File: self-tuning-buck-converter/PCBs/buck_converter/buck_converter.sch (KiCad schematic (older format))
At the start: 35 parts, among them Q1 NMOS, U1 LT1999-50, U2 LM7322, U3 IR2125, U4 ESP32-DEVKITC-32D

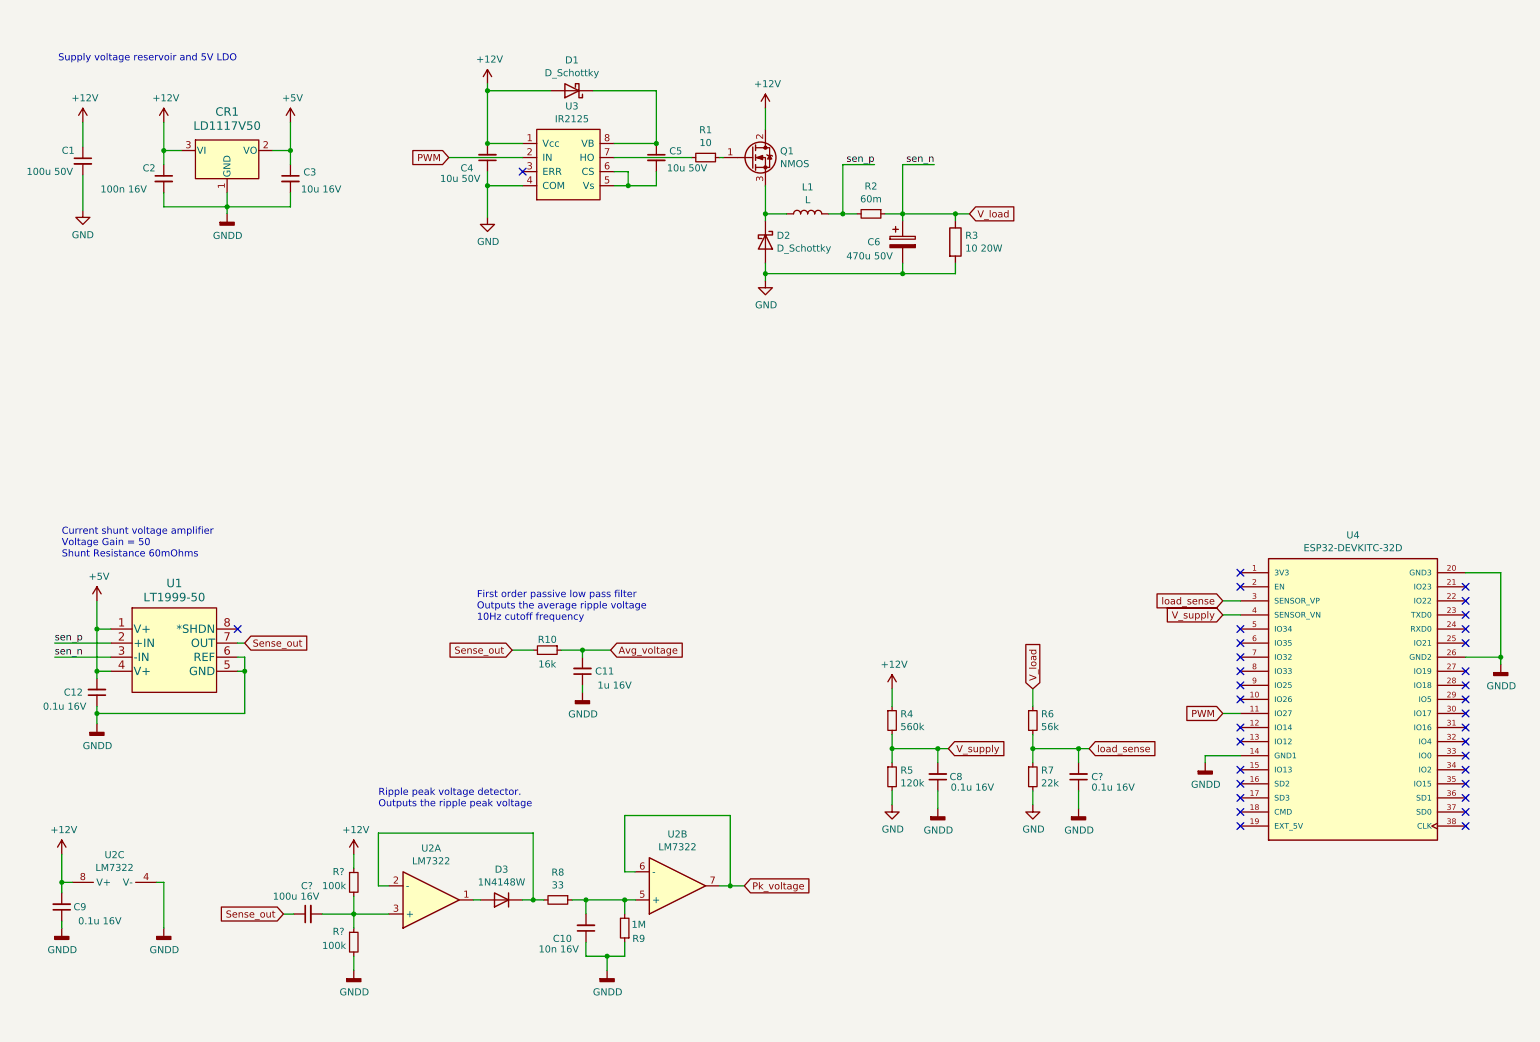
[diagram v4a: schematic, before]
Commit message: Finalised PCM and selected component footprints
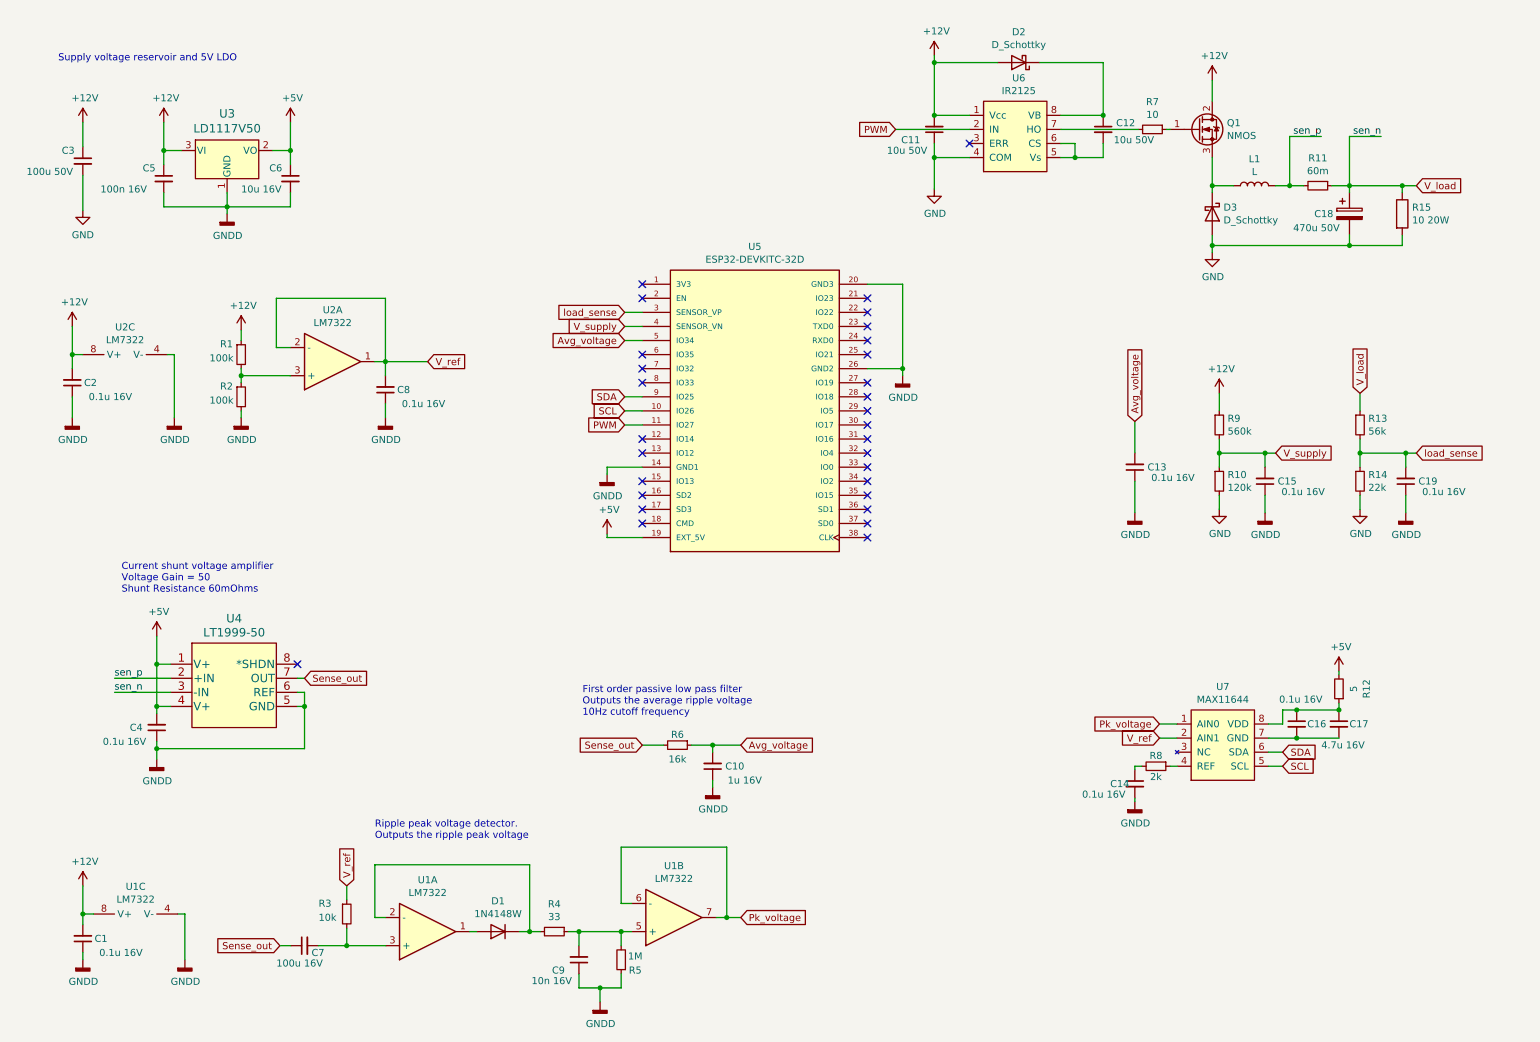
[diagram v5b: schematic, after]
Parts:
- removed CR1: LD1117V50, TO-220_STM, symbol LD1117V50:LD1117V50
- added C13, C14, C16, C2, C8: 0.1u 16V, Capacitor_SMD:C_0603_1608Metric_Pad1.08x0.95mm_HandSolder, symbol Device:C_Small
- added C17: 4.7u 16V, Capacitor_SMD:C_0603_1608Metric_Pad1.08x0.95mm_HandSolder, symbol Device:C_Small
- added R12: 5, Resistor_SMD:R_0603_1608Metric_Pad0.98x0.95mm_HandSolder, symbol Device:R_Small
- added R3: 10k, Resistor_SMD:R_0603_1608Metric_Pad0.98x0.95mm_HandSolder, symbol Device:R_Small
- added R8: 2k, Resistor_SMD:R_0603_1608Metric_Pad0.98x0.95mm_HandSolder, symbol Device:R_Small
- added U2: LM7322, Package_SO:SOIC-8_3.9x4.9mm_P1.27mm, symbol Device:Opamp_Dual_Generic
- added U3: LD1117V50, Package_TO_SOT_THT:TO-220-3_Vertical, symbol LD1117V50:LD1117V50
- added U7: MAX11644, Package_SO:MSOP-8_3x3mm_P0.65mm, symbol MAX11644:MAX11644
- C1: renamed from C9; footprint (none) -> Capacitor_SMD:C_0603_1608Metric_Pad1.08x0.95mm_HandSolder
- C10: renamed from C11; footprint (none) -> Capacitor_SMD:C_0603_1608Metric_Pad1.08x0.95mm_HandSolder
- C11: renamed from C4; footprint (none) -> Capacitor_THT:CP_Radial_D5.0mm_P2.00mm; Part Number (none) -> 860010672009
- C12: renamed from C5; footprint (none) -> Capacitor_THT:CP_Radial_D5.0mm_P2.00mm; Part Number (none) -> 860010672009
- C15: renamed from C8; footprint (none) -> Capacitor_SMD:C_0603_1608Metric_Pad1.08x0.95mm_HandSolder
- C19: renamed from C?; footprint (none) -> Capacitor_SMD:C_0603_1608Metric_Pad1.08x0.95mm_HandSolder
- C3: renamed from C1; footprint (none) -> Capacitor_THT:CP_Radial_D10.0mm_P5.00mm; Part Number (none) -> 860010675020
- C4: renamed from C12; footprint (none) -> Capacitor_SMD:C_0603_1608Metric_Pad1.08x0.95mm_HandSolder
- C5: renamed from C2; footprint (none) -> Capacitor_SMD:C_0603_1608Metric_Pad1.08x0.95mm_HandSolder
- C6: renamed from C3; footprint (none) -> Capacitor_SMD:C_0805_2012Metric_Pad1.18x1.45mm_HandSolder
- C7: renamed from C?; footprint (none) -> Capacitor_THT:CP_Radial_D8.0mm_P3.50mm; Part Number (none) -> 860020374012
- C9: renamed from C10; footprint (none) -> Capacitor_SMD:C_0603_1608Metric_Pad1.08x0.95mm_HandSolder
- D1: renamed from D3; footprint Diode_SMD:D_SOD-123 -> Diode_THT:D_DO-35_SOD27_P7.62mm_Horizontal
- D2: renamed from D1; footprint (none) -> Diode_THT:D_A-405_P12.70mm_Horizontal
- D3: renamed from D2; footprint (none) -> Diode_THT:D_A-405_P12.70mm_Horizontal
- Q1: footprint (none) -> Package_TO_SOT_THT:TO-220-3_Vertical
- R1, R2: renamed from R?; footprint (none) -> Resistor_SMD:R_0603_1608Metric_Pad0.98x0.95mm_HandSolder
- R10: renamed from R5; footprint (none) -> Resistor_SMD:R_0603_1608Metric_Pad0.98x0.95mm_HandSolder
- R13: renamed from R6; footprint (none) -> Resistor_SMD:R_0603_1608Metric_Pad0.98x0.95mm_HandSolder
- R14: renamed from R7; footprint (none) -> Resistor_SMD:R_0603_1608Metric_Pad0.98x0.95mm_HandSolder
- R4: renamed from R8; footprint (none) -> Resistor_SMD:R_0603_1608Metric_Pad0.98x0.95mm_HandSolder
- R5: renamed from R9; footprint (none) -> Resistor_SMD:R_0603_1608Metric_Pad0.98x0.95mm_HandSolder
- R7: renamed from R1; footprint (none) -> Resistor_SMD:R_0603_1608Metric_Pad0.98x0.95mm_HandSolder
- R9: renamed from R4; footprint (none) -> Resistor_SMD:R_0603_1608Metric_Pad0.98x0.95mm_HandSolder
- U1: renamed from U2; footprint (none) -> Package_SO:SOIC-8_3.9x4.9mm_P1.27mm
- U4: renamed from U1; footprint MSOP_8_ADI -> Package_SO:SOIC-8_3.9x4.9mm_P1.27mm
- U6: renamed from U3; footprint (none) -> Package_DIP:DIP-8_W7.62mm
- renumbered C6 to C18, R2 to R11, R3 to R15, R10 to R6, U4 to U5
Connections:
- net +12V: now also C2.2, U2.8 (V+), U3.3 (VI)
- net +5V: now also U5.19 (EXT_5V), R12.2, U3.2 (VO)
- net Avg_voltage: now also U5.5 (IO34), C13.2
- net GNDD: now also C13.1, C14.2, C2.1, C8.1, U2.4 (V-), U3.1 (GND)
- net Pk_voltage: now also U7.1 (AIN0)
- net SCL: now reaches U5.10 (IO26)
- net SCL: now also U7.5 (SCL)
- net SDA: now reaches U5.9 (IO25)
- net SDA: now also U7.6 (SDA)
- net at R1.2, R2.1: now also U2.3 (+); no longer C7.2, U1.3 (+)
- new net: C7.2, R3.2, U1.3 (+)
- new net: R8.1, U7.4 (REF)
- new net: C16.2, C17.2, U7.7 (GND)
- new net: C16.1, C17.1, R12.1, U7.8 (VDD)
- new net: C14.1, R8.2
- new net V_ref: C8.2, R3.1, U2.1, U2.2 (-), U7.2 (AIN1)
- no-connect marks 34 -> 30
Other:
- moved on the sheet: C1, C10, C11, C12, C15, C18, C19, C4, C7, C9, D1, D2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

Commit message: Updated schematic with edits found from building it in the lab
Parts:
- removed R4: 33, Resistor_SMD:R_0603_1608Metric_Pad0.98x0.95mm_HandSolder, symbol Device:R_Small
- removed unit 2 of U1
- removed U2: LM7322, Package_SO:SOIC-8_3.9x4.9mm_P1.27mm, symbol Device:Opamp_Dual_Generic
- added RV1: 100, Potentiometer_THT:Potentiometer_Bourns_3266Y_Vertical, symbol Device:R_POT
- added U1: AMP from lab, Package_DIP:DIP-14_W7.62mm, symbol Device:Opamp_Quad_Generic
- C11, C12: symbol Device:C_Small -> Device:CP_Small
- C9: value 10n 16V -> 100n 16V
- D2, D3: footprint Diode_THT:D_A-405_P12.70mm_Horizontal -> Diode_THT:D_A-405_P7.62mm_Horizontal
- renumbered C2 to C1, C18 to C16, C16 to C17, C19 to C18, C17 to C19, C4 to C2, C1 to C4, R11 to R10, R13 to R11, R14 to R12, R15 to R13, R12 to R14, R5 to R4, R6 to R5, R7 to R6, R9 to R7, R10 to R8, R8 to R9, U1 to U2, U4 to U3, U3 to U4, U5 to U6, U6 to U7, U7 to U8
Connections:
- net +12V: now also C11.1, U1.11 (V-); no longer C11.2
- net GND: now also C11.2; no longer C11.1
- net GNDD: now also U1.4 (V+)
- net Pk_voltage: now also U1.5 (+), U1.7
- net V_ref: now also U1.1, U1.3 (+)
- net at D3.1 (K), L1.1, Q1.3 (S): now also C12.2, U7.5 (Vs), U7.6 (CS)
- net at R1.2, R2.1: now also U1.2 (-)
- net at D1.1 (K), U2.2 (-): now also RV1.1
- net at C9.2, R4.2: now also RV1.2, U1.6 (-)
- no-connect marks 30 -> 31
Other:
- note added: "Supply voltage (VCC) reservoir, 5V LDO, and VCC/2 refrence voltage"
- note removed: "Supply voltage reservoir and 5V LDO"
- moved on the sheet: C1, C10, C13, C14, C15, C16, C17, C18, C19, C2, C3, C5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

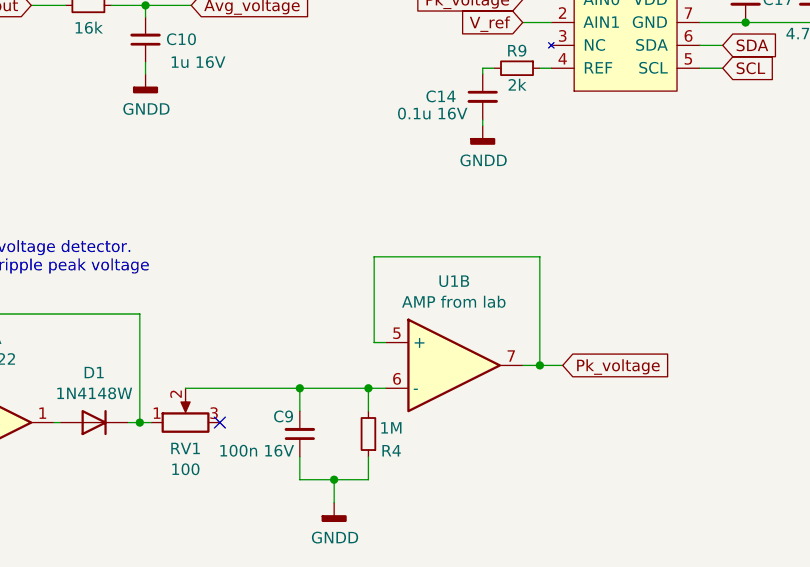
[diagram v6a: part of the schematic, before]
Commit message: PEak detection evaluation
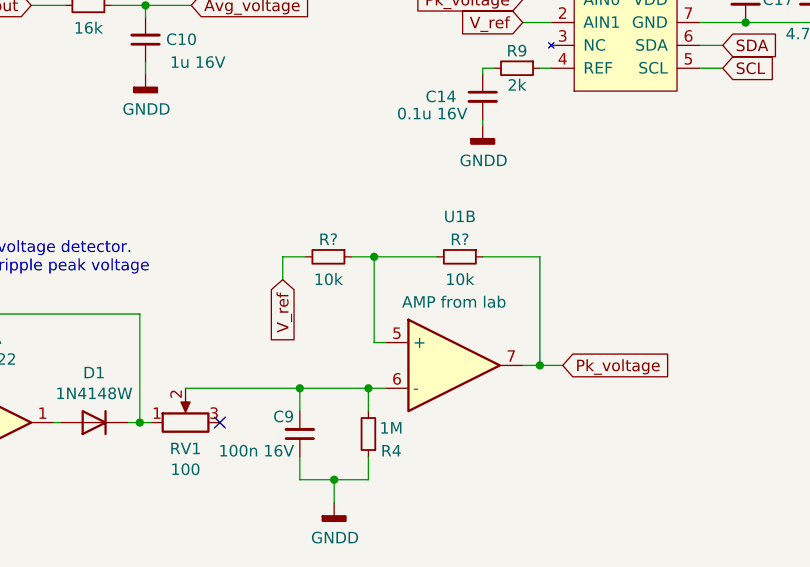
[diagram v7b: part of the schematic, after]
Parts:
- added R? (x2): 10k, Resistor_SMD:R_0603_1608Metric_Pad0.98x0.95mm_HandSolder, symbol Device:R_Small
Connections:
- net Pk_voltage: now also R?.1; no longer U1.5 (+)
- net V_ref: now also R?.2
- new net: R?.1, R?.2, U1.5 (+)
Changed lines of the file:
@@
 U 2 1 6162B04C
 P 5475 6800
-F 0 "U1" H 5475 7167 50  0000 C CNN
+F 0 "U1" H 5500 7450 50  0000 C CNN
 F 1 "AMP from lab" H 5475 7076 50  0000 C CNN
 F 2 "Package_DIP:DIP-14_W7.62mm" H 5475 6800 50  0001 C CNN
@@
 Wire Wire Line
 	5850 6800 5850 6325
-Wire Wire Line
-	5850 6325 5125 6325
 Wire Wire Line
 	5775 6800 5850 6800
@@
 Connection ~ 5300 3350
 Connection ~ 6175 3350
+$Comp
+L Device:R_Small R?
+U 1 1 6151C957
+P 4925 6325
+F 0 "R?" V 4850 6325 50  0000 C CNN
+F 1 "10k" V 5025 6325 50  0000 C CNN
+F 2 "Resistor_SMD:R_0603_1608Metric_Pad0.98x0.95mm_HandSolder" H 4925 6325 50  0001 C CNN
+F 3 "~" H 4925 6325 50  0001 C CNN
+F 4 "RR0816P-163-D" V 4925 6325 50  0001 C CNN "Part Number"
+	1    4925 6325
+	0    1    1    0
+$EndComp
+$Comp
+L Device:R_Small R?
+U 1 1 6151D31C
+P 5500 6325
+F 0 "R?" V 5425 6325 50  0000 C CNN
+F 1 "10k" V 5600 6325 50  0000 C CNN
+F 2 "Resistor_SMD:R_0603_1608Metric_Pad0.98x0.95mm_HandSolder" H 5500 6325 50  0001 C CNN
+F 3 "~" H 5500 6325 50  0001 C CNN
+F 4 "RR0816P-163-D" V 5500 6325 50  0001 C CNN "Part Number"
+	1    5500 6325
+	0    1    1    0
+$EndComp
+Wire Wire Line
+	5850 6325 5600 6325
+Wire Wire Line
+	5400 6325 5125 6325
+Wire Wire Line
+	5125 6325 5025 6325
+Connection ~ 5125 6325
+Wire Wire Line
+	4825 6325 4725 6325
+Wire Wire Line
+	4725 6325 4725 6425
+Text GLabel 4725 6425 3    50   Input ~ 0
+V_ref
 $EndSCHEMATC
